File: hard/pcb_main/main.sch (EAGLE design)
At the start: 224 parts

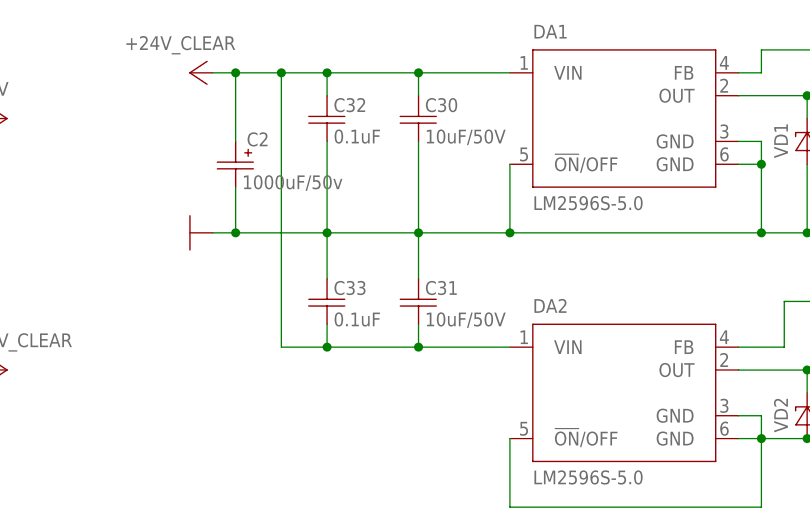
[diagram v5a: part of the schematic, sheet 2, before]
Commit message: placed outputs and power supplys
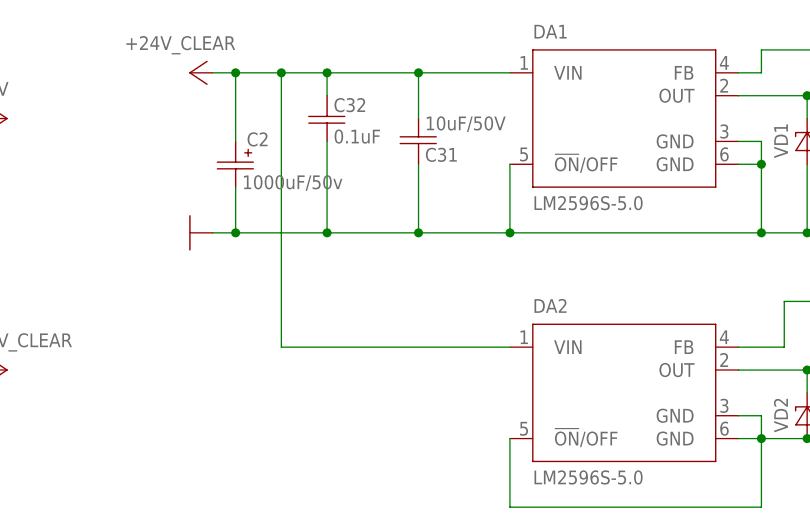
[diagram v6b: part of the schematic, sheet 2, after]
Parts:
- removed C30: 10uF/50V, rcl:C-EUC2220K
- removed C33: 0.1uF, rcl:C-EUC0603
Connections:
- net +24V_CLEAR: no longer C30.1, C33.2
- net GND: no longer C30.2, C33.1
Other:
- moved on the sheet: C31
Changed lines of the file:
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@@
 <attribute name="PARTNO" value="1812L200DR"/>
-</part>
-<part name="C30" library="rcl" deviceset="C-EU" device="C2220K" value="10uF/50V">
-<attribute name="PARTNO" value="22205C106KAT2A"/>
 </part>
 <part name="C31" library="rcl" deviceset="C-EU" device="C2220K" value="10uF/50V">
@@
 </part>
 <part name="C32" library="rcl" deviceset="C-EU" device="C0603" value="0.1uF">
-<attribute name="PARTNO" value="C0603C104K5RACTU"/>
-</part>
-<part name="C33" library="rcl" deviceset="C-EU" device="C0603" value="0.1uF">
 <attribute name="PARTNO" value="C0603C104K5RACTU"/>
 </part>
@@
 <attribute name="PARTNO" value="1812L200DR" x="259.08" y="177.8" size="1.27" layer="96" display="off"/>
 </instance>
-<instance part="C30" gate="G$1" x="185.42" y="175.26">
-<attribute name="PARTNO" x="185.42" y="175.26" size="1.27" layer="96" display="off"/>
-</instance>
-<instance part="C31" gate="G$1" x="185.42" y="154.94">
-<attribute name="PARTNO" x="185.42" y="154.94" size="1.27" layer="96" display="off"/>
+<instance part="C31" gate="G$1" x="185.42" y="172.72" rot="MR180">
+<attribute name="PARTNO" x="185.42" y="172.72" size="1.27" layer="96" rot="MR180" display="off"/>
 </instance>
 <instance part="C32" gate="G$1" x="175.26" y="175.26">
 <attribute name="PARTNO" value="C0603C104K5RACTU" x="175.26" y="175.26" size="1.524" layer="96" display="off"/>
-</instance>
-<instance part="C33" gate="G$1" x="175.26" y="154.94">
-<attribute name="PARTNO" value="C0603C104K5RACTU" x="175.26" y="154.94" size="1.524" layer="96" display="off"/>
 </instance>
 </instances>
@@
 <wire x1="175.26" y1="172.72" x2="175.26" y2="162.56" width="0.1524" layer="91"/>
 <junction x="175.26" y="162.56"/>
-<pinref part="C30" gate="G$1" pin="2"/>
-<wire x1="185.42" y1="172.72" x2="185.42" y2="162.56" width="0.1524" layer="91"/>
 <junction x="185.42" y="162.56"/>
 <pinref part="C31" gate="G$1" pin="1"/>
-<wire x1="185.42" y1="157.48" x2="185.42" y2="162.56" width="0.1524" layer="91"/>
-<pinref part="C33" gate="G$1" pin="1"/>
-<wire x1="175.26" y1="157.48" x2="175.26" y2="162.56" width="0.1524" layer="91"/>
+<wire x1="185.42" y1="170.18" x2="185.42" y2="162.56" width="0.1524" layer="91"/>
 </segment>
 <segment>
@@
 <wire x1="175.26" y1="180.34" x2="185.42" y2="180.34" width="0.1524" layer="91"/>
 <wire x1="185.42" y1="180.34" x2="195.58" y2="180.34" width="0.1524" layer="91"/>
-<wire x1="195.58" y1="149.86" x2="185.42" y2="149.86" width="0.1524" layer="91"/>
-<wire x1="185.42" y1="149.86" x2="175.26" y2="149.86" width="0.1524" layer="91"/>
-<wire x1="175.26" y1="149.86" x2="170.18" y2="149.86" width="0.1524" layer="91"/>
+<wire x1="195.58" y1="149.86" x2="170.18" y2="149.86" width="0.1524" layer="91"/>
 <wire x1="170.18" y1="149.86" x2="170.18" y2="180.34" width="0.1524" layer="91"/>
 <junction x="170.18" y="180.34"/>
@@
 <wire x1="165.1" y1="180.34" x2="162.56" y2="180.34" width="0.1524" layer="91"/>
 <junction x="165.1" y="180.34"/>
-<pinref part="C30" gate="G$1" pin="1"/>
-<wire x1="185.42" y1="177.8" x2="185.42" y2="180.34" width="0.1524" layer="91"/>
-<junction x="185.42" y="180.34"/>
 <pinref part="C32" gate="G$1" pin="1"/>
 <wire x1="175.26" y1="177.8" x2="175.26" y2="180.34" width="0.1524" layer="91"/>
 <junction x="175.26" y="180.34"/>
 <pinref part="C31" gate="G$1" pin="2"/>
-<wire x1="185.42" y1="152.4" x2="185.42" y2="149.86" width="0.1524" layer="91"/>
-<junction x="185.42" y="149.86"/>
-<pinref part="C33" gate="G$1" pin="2"/>
-<wire x1="175.26" y1="152.4" x2="175.26" y2="149.86" width="0.1524" layer="91"/>
-<junction x="175.26" y="149.86"/>
-</segment>
-<segment>
+<wire x1="185.42" y1="175.26" x2="185.42" y2="180.34" width="0.1524" layer="91"/>
+<junction x="185.42" y="180.34"/>
+</segment>
+<segment>

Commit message: discrete inputs 1..16 routed
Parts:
- added C30, C33, C35, C36, C37, C38, C39, C40, C41, C42, C43, C44, C45, C46, C47, C48: 0.1uF, rcl:C-EUC0603
- added D11, D12, D13, D14: TCMT4100, optocoupler:TCMT4100
- added D15: AUIPS7111S, transistor-fet:AUIPS7111S
- added R100, R104, R107, R110, R113, R116, R119, R128, R129, R130, R131, R140, R141, R142, R143, R94: 10kOhm, rcl:R-EU_R0603
- added R101, R102, R105, R108, R111, R114, R117, R120, R121, R122, R123, R132, R133, R134, R135, R95: 4.7kOhm, rcl:R-EU_R1206
- added R103, R106, R109, R112, R115, R118, R124, R125, R126, R127, R136, R137, R138, R139, R93, R99: 1kOhm, rcl:R-EU_R2512
- added R96, R98: 1kOhm, rcl:R-EU_R0805
- added R97: 100Ohm, rcl:R-EU_R0603
- added VD60, VD64, VD66, VD68, VD70, VD72, VD74, VD76, VD78, VD80, VD82, VD84, VD86, VD88, VD90, VD92: SM6T200A, diode:DIODE-TVS-UNIDIR-SMB
- added VD61, VD65, VD67, VD69, VD71, VD73, VD75, VD77, VD79, VD81, VD83, VD85, VD87, VD89, VD91, VD93: 400V, diode:DIODE-STANDARD-SMA
- added VD62, VD63: (no value), diode:DIODE-STANDARD-SOD323
- added VT2: BC817-16SMD, transistor-npn:BC817-16SMD
- VD22: value SM6T220A -> SM6T200A; PARTNO SM6T220A -> SM6T200A
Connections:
- new net DISCRETE_1: C30.1, D12.1.TC, R94.2
- new net DISCRETE_10: C42.1, D13.2.TC, R129.2
- new net DISCRETE_11: C43.1, D13.3.TC, R130.2
- new net DISCRETE_12: C44.1, D13.4.TC, R131.2
- new net DISCRETE_13: C45.1, D14.1.TC, R140.2
- new net DISCRETE_14: C46.1, D14.2.TC, R141.2
- new net DISCRETE_15: C47.1, D14.3.TC, R142.2
- new net DISCRETE_16: C48.1, D14.4.TC, R143.2
- new net DISCRETE_2: C33.1, D12.2.TC, R100.2
- new net DISCRETE_3: C35.1, D12.3.TC, R104.2
- new net DISCRETE_4: C36.1, D12.4.TC, R107.2
- new net DISCRETE_5: C37.1, D11.1.TC, R110.2
- new net DISCRETE_6: C38.1, D11.2.TC, R113.2
- new net DISCRETE_7: C39.1, D11.3.TC, R116.2
- new net DISCRETE_8: C40.1, D11.4.TC, R119.2
- new net DISCRETE_9: C41.1, D13.1.TC, R128.2
- new net N$100: D11.4.DA, R117.2
- new net N$101: D13.1.DA, R120.2
- new net N$102: D13.2.DA, R121.2
- new net N$103: D13.3.DA, R122.2
- new net N$104: D13.4.DA, R123.2
- new net N$105: D14.1.DA, R132.2
- new net N$106: D14.2.DA, R133.2
- new net N$107: D14.3.DA, R134.2
- new net N$108: D14.4.DA, R135.2
- new net N$109: R99.2, VD65.C
- new net N$111: R103.2, VD67.C
- new net N$113: R106.2, VD69.C
- new net N$115: R109.2, VD71.C
- new net N$117: R112.2, VD73.C
- new net N$119: R115.2, VD75.C
- new net N$121: R118.2, VD77.C
- new net N$123: R124.2, VD79.C
- new net N$125: R125.2, VD81.C
- new net N$127: R126.2, VD83.C
- new net N$129: R127.2, VD85.C
- new net N$131: R136.2, VD87.C
- new net N$133: R137.2, VD89.C
- new net N$135: R138.2, VD91.C
- new net N$137: R139.2, VD93.C
- new net N$87: R97.1, VT2.B
- new net N$88: D15.IN, R96.2
- new net N$89: R96.1, VD62.C, VT2.C
- new net N$90: D15.IFB, VD63.A
- new net N$91: D12.1.DA, R95.2
- new net N$92: R98.2, VD63.C
- new net N$93: D12.2.DA, R101.2
- new net N$94: D12.3.DA, R102.2
- new net N$95: D12.4.DA, R105.2
- new net N$96: R93.2, VD61.C
- new net N$97: D11.1.DA, R108.2
- new net N$98: D11.2.DA, R111.2
- new net N$99: D11.3.DA, R114.2
- new net RAW_DISCRETE_1: R93.1, R95.1, VD60.C, XP5.1
- new net RAW_DISCRETE_10: R121.1, R125.1, VD80.C, XP5.10
- new net RAW_DISCRETE_11: R122.1, R126.1, VD82.C, XP5.11
- new net RAW_DISCRETE_12: R123.1, R127.1, VD84.C, XP5.12
- new net RAW_DISCRETE_13: R132.1, R136.1, VD86.C, XP5.13
- new net RAW_DISCRETE_14: R133.1, R137.1, VD88.C, XP5.14
- new net RAW_DISCRETE_15: R134.1, R138.1, VD90.C, XP5.15
- new net RAW_DISCRETE_16: R135.1, R139.1, VD92.C, XP5.16
- new net RAW_DISCRETE_2: R101.1, R99.1, VD64.C, XP5.2
- new net RAW_DISCRETE_3: R102.1, R103.1, VD66.C, XP5.3
- new net RAW_DISCRETE_4: R105.1, R106.1, VD68.C, XP5.4
- new net RAW_DISCRETE_5: R108.1, R109.1, VD70.C, XP5.5
- new net RAW_DISCRETE_6: R111.1, R112.1, VD72.C, XP5.6
- new net RAW_DISCRETE_7: R114.1, R115.1, VD74.C, XP5.7
- new net RAW_DISCRETE_8: R117.1, R118.1, VD76.C, XP5.8
- new net RAW_DISCRETE_9: R120.1, R124.1, VD78.C, XP5.9
- new net Z_CHECK: D15.OUT1, D15.OUT2, VD61.A, VD65.A, VD67.A, VD69.A, VD71.A, VD73.A, VD75.A, VD77.A, VD79.A, VD81.A, VD83.A, VD85.A, VD87.A, VD89.A, VD91.A, VD93.A
- new net Z_CHECK_TOGGLE: R97.2
- net +24V_CLEAR: now also D15.VCC
- net +3V3: now also R100.1, R104.1, R107.1, R110.1, R113.1, R116.1, R119.1, R128.1, R129.1, R130.1, R131.1, R140.1, R141.1, R142.1, R143.1, R94.1
- net GND: now also C30.2, C33.2, C35.2, C36.2, C37.2, C38.2, C39.2, C40.2, C41.2, C42.2, C43.2, C44.2, C45.2, C46.2, C47.2, C48.2, D11.1.DC, D11.1.TE, D11.2.DC, D11.2.TE, D11.3.DC, D11.3.TE, D11.4.DC, D11.4.TE, D12.1.DC, D12.1.TE, D12.2.DC, D12.2.TE, D12.3.DC, D12.3.TE, D12.4.DC, D12.4.TE, D13.1.DC, D13.1.TE, D13.2.DC, D13.2.TE, D13.3.DC, D13.3.TE, D13.4.DC, D13.4.TE, D14.1.DC, D14.1.TE, D14.2.DC, D14.2.TE, D14.3.DC, D14.3.TE, D14.4.DC, D14.4.TE, R98.1, VD60.A, VD62.A, VD64.A, VD66.A, VD68.A, VD70.A, VD72.A, VD74.A, VD76.A, VD78.A, VD80.A, VD82.A, VD84.A, VD86.A, VD88.A, VD90.A, VD92.A, VT2.E
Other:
- moved on the sheet: VD22, XP2, XP3, XP4, XP5

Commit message: discrete inputs improvements
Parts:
- removed XP5: DISCRETE(33..48), connector:TYCO-174053(2.54)
- added XP13: DISCRETE(33..48), connector:PLD_2X8
- XP3, XP4: device connector:TYCO-174053(2.54) -> connector:PLD_2X8
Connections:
- net RAW_DISCRETE_1: now also XP13.1; no longer XP5.1
- net RAW_DISCRETE_10: now also XP13.10; no longer XP5.10
- net RAW_DISCRETE_11: now also XP13.11; no longer XP5.11
- net RAW_DISCRETE_12: now also XP13.12; no longer XP5.12
- net RAW_DISCRETE_13: now also XP13.13; no longer XP5.13
- net RAW_DISCRETE_14: now also XP13.14; no longer XP5.14
- net RAW_DISCRETE_15: now also XP13.15; no longer XP5.15
- net RAW_DISCRETE_16: now also XP13.16; no longer XP5.16
- net RAW_DISCRETE_2: now also XP13.2; no longer XP5.2
- net RAW_DISCRETE_3: now also XP13.3; no longer XP5.3
- net RAW_DISCRETE_4: now also XP13.4; no longer XP5.4
- net RAW_DISCRETE_5: now also XP13.5; no longer XP5.5
- net RAW_DISCRETE_6: now also XP13.6; no longer XP5.6
- net RAW_DISCRETE_7: now also XP13.7; no longer XP5.7
- net RAW_DISCRETE_8: now also XP13.8; no longer XP5.8
- net RAW_DISCRETE_9: now also XP13.9; no longer XP5.9
